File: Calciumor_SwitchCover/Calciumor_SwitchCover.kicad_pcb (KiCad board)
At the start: 2 copper layers, 77 x 96 mm, 21 parts

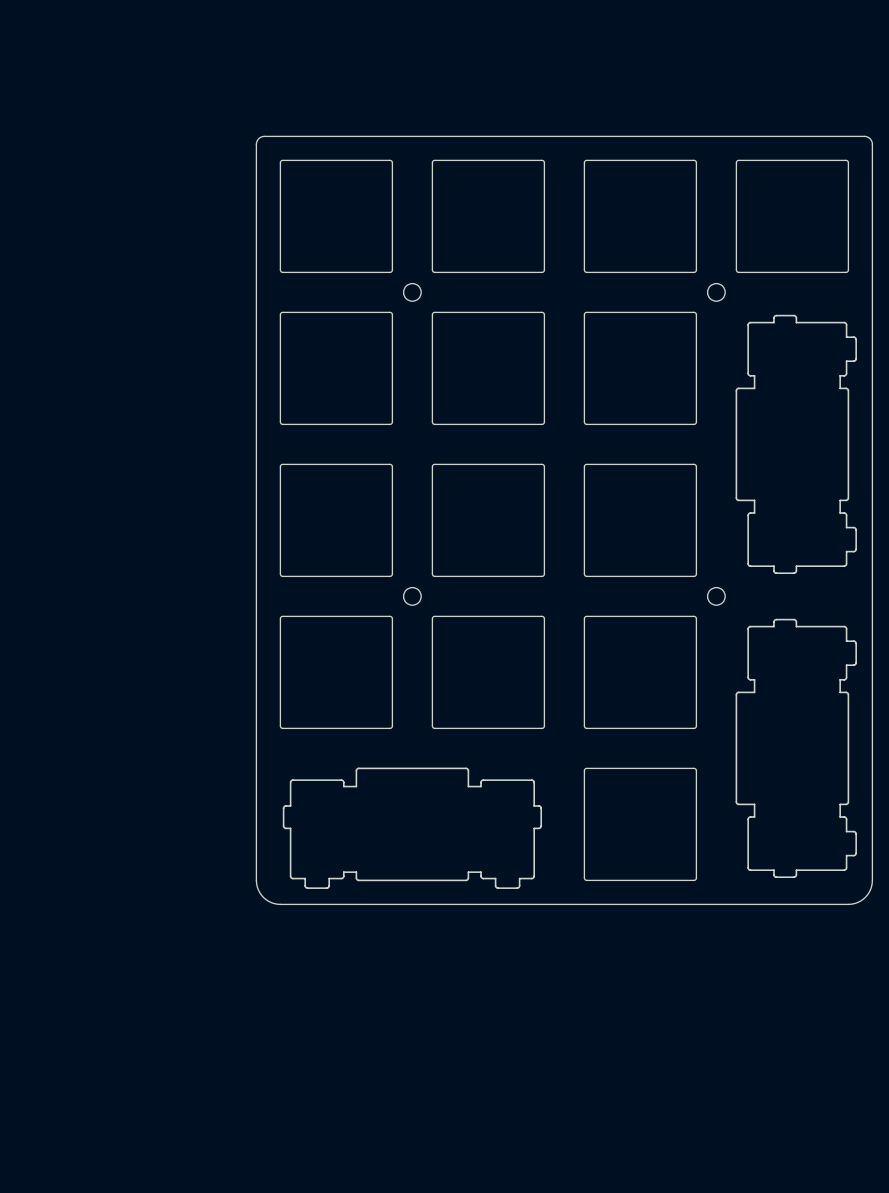
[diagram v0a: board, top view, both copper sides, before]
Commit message: Fixed 2V5 Power supply
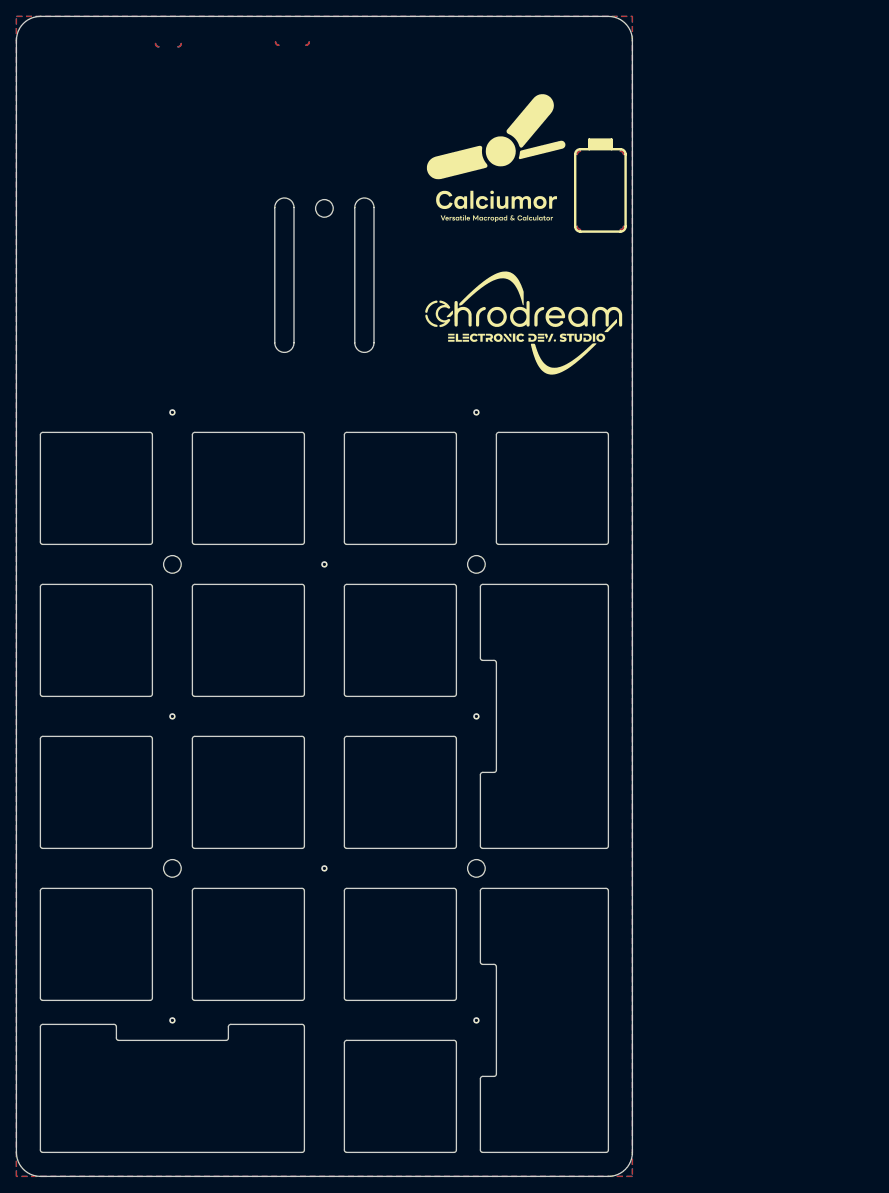
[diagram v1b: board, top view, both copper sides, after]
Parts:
- added G***: LOGO, Calciumor:Calciumor, F.Cu at (130.0, 52.5)
- added G***: LOGO, Ultramarine-2:Chrodream_logo, F.Cu at (133.5, 73.0)
- added H24: MountingHole, MountingHole:MountingHole_2.2mm_M2, F.Cu at (108.5, 59.0)
- moved H1 45.3 mm to (80.0, 94.0)
- moved H10 45.3 mm to (99.0, 132.0)
- moved H11 45.3 mm to (118.0, 132.0)
- moved H12 45.3 mm to (80.0, 151.0)
- moved H13 45.3 mm to (99.0, 151.0)
- moved H14 45.3 mm to (118.0, 151.0)
- moved H15 45.3 mm to (137.0, 160.5)
- moved H16 45.3 mm to (89.5, 170.0)
- moved H17 45.3 mm to (118.0, 170.0)
- moved H18 45.3 mm to (89.5, 103.5)
- moved H19 45.3 mm to (127.5, 103.5)
- moved H2 45.3 mm to (99.0, 94.0)
- moved H20 45.3 mm to (89.5, 141.5)
- moved H21 45.3 mm to (127.5, 141.5)
- moved H3 45.3 mm to (118.0, 94.0)
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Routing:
- net Earth: vias 0 -> 8
- added copper zone on B.Cu, net Earth
- added copper zone on F.Cu, net Earth
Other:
- board size 77 x 96 mm -> 77 x 145 mm

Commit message: Changed to native USB
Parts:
- G***: moved to B.Cu
- moved G*** 12.2 mm to (128.0, 64.5)
- moved G*** 10.2 mm to (129.6, 63.6), turned to 90 degrees
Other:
- outline, holes or cut-outs redrawn

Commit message: Core_rev1.0
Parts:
- added H23: MountingHole, MountingHole:MountingHole_2.2mm_M2, F.Cu at (103.5, 50.0)
- H15, H16, H17, H8: value Switch Hole -> Switch Hole 2u
- moved G*** 11.6 mm to (136.5, 72.3), turned to 90 degrees
- moved H24 10.3 mm to (113.5, 50.0)
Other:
- outline, holes or cut-outs redrawn

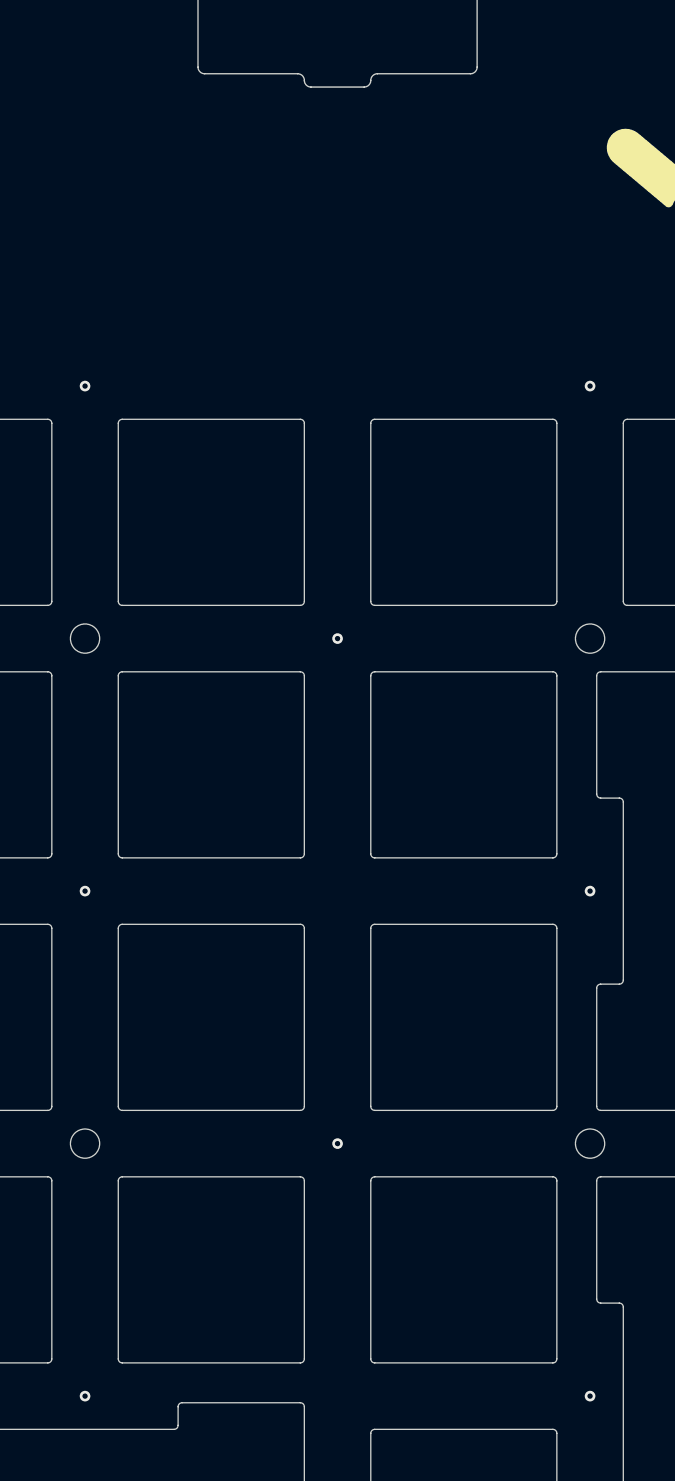
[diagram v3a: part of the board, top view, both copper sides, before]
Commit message: Under cover completed
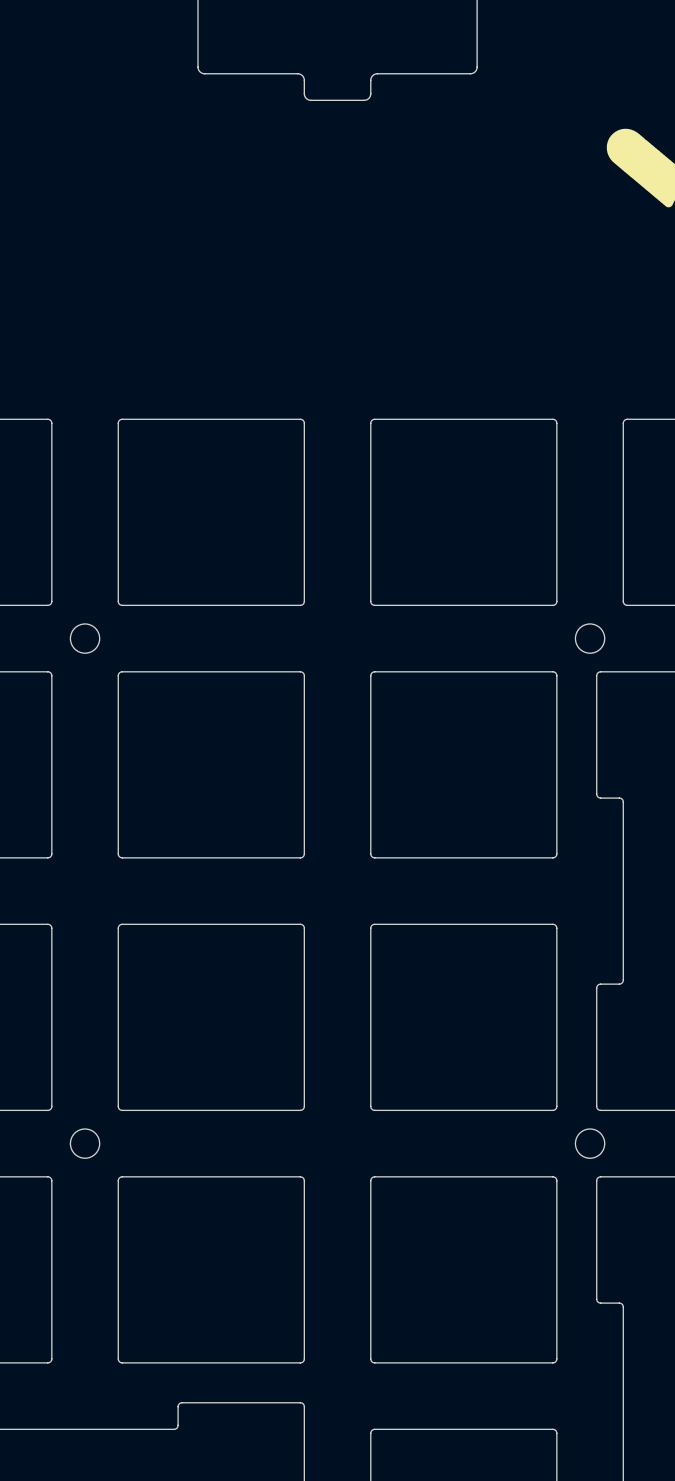
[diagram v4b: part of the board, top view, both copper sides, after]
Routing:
- net Earth: vias 8 -> 0
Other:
- outline, holes or cut-outs redrawn
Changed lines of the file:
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@@
 	)
 	(gr_line
-		(start 106.5 62)
-		(end 110.5 62)
-		(stroke
-			(width 0.1)
-			(type default)
-		)
-		(layer "Edge.Cuts")
-	)
-	(gr_arc
-		(start 106.5 62)
-		(mid 106.146447 61.853553)
-		(end 106 61.5)
+		(start 106.5 63)
+		(end 110.5 63)
+		(stroke
+			(width 0.1)
+			(type default)
+		)
+		(layer "Edge.Cuts")
+	)
+	(gr_arc
+		(start 106.5 63)
+		(mid 106.146447 62.853553)
+		(end 106 62.5)
+		(stroke
+			(width 0.1)
+			(type default)
+		)
+		(layer "Edge.Cuts")
+	)
+	(gr_line
+		(start 111 61.5)
+		(end 111 62.5)
+		(stroke
+			(width 0.1)
+			(type default)
+		)
+		(layer "Edge.Cuts")
+	)
+	(gr_line
+		(start 106 61.5)
+		(end 106 62.5)
 		(stroke
 			(width 0.1)
@@
 	)
 	(gr_arc
-		(start 111 61.5)
-		(mid 110.853553 61.853553)
-		(end 110.5 62)
+		(start 111 62.5)
+		(mid 110.853553 62.853553)
+		(end 110.5 63)
 		(stroke
 			(width 0.1)
@@
 		(layer "F.Fab")
 	)
-	(via
-		(at 108.5 103.5)
-		(size 0.8)
-		(drill 0.4)
-		(layers "F.Cu" "B.Cu")
-		(free yes)
-		(net 1)
-	)
-	(via
-		(at 127.5 122.5)
-		(size 0.8)
-		(drill 0.4)
-		(layers "F.Cu" "B.Cu")
-		(free yes)
-		(net 1)
-	)
-	(via
-		(at 89.5 84.5)
-		(size 0.8)
-		(drill 0.4)
-		(layers "F.Cu" "B.Cu")
-		(free yes)
-		(net 1)
-	)
-	(via
-		(at 89.5 160.5)
-		(size 0.8)
-		(drill 0.4)
-		(layers "F.Cu" "B.Cu")
-		(free yes)
-		(net 1)
-	)
-	(via
-		(at 127.5 84.5)
-		(size 0.8)
-		(drill 0.4)
-		(layers "F.Cu" "B.Cu")
-		(free yes)
-		(net 1)
-	)
-	(via
-		(at 108.5 141.5)
-		(size 0.8)
-		(drill 0.4)
-		(layers "F.Cu" "B.Cu")
-		(free yes)
-		(net 1)
-	)
-	(via
-		(at 127.5 160.5)
-		(size 0.8)
-		(drill 0.4)
-		(layers "F.Cu" "B.Cu")
-		(free yes)
-		(net 1)
-	)
-	(via
-		(at 89.5 122.5)
-		(size 0.8)
-		(drill 0.4)
-		(layers "F.Cu" "B.Cu")
-		(free yes)
-		(net 1)
-	)
 	(zone
